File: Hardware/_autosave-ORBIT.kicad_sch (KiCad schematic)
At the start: 52 parts, among them J1 West Connector, J2 East Connector, U1 MCP73031, U10 8MHz, U15 TPS63802DLAR, U16 STM32F030C8Tx, U22 CP2102-GMR

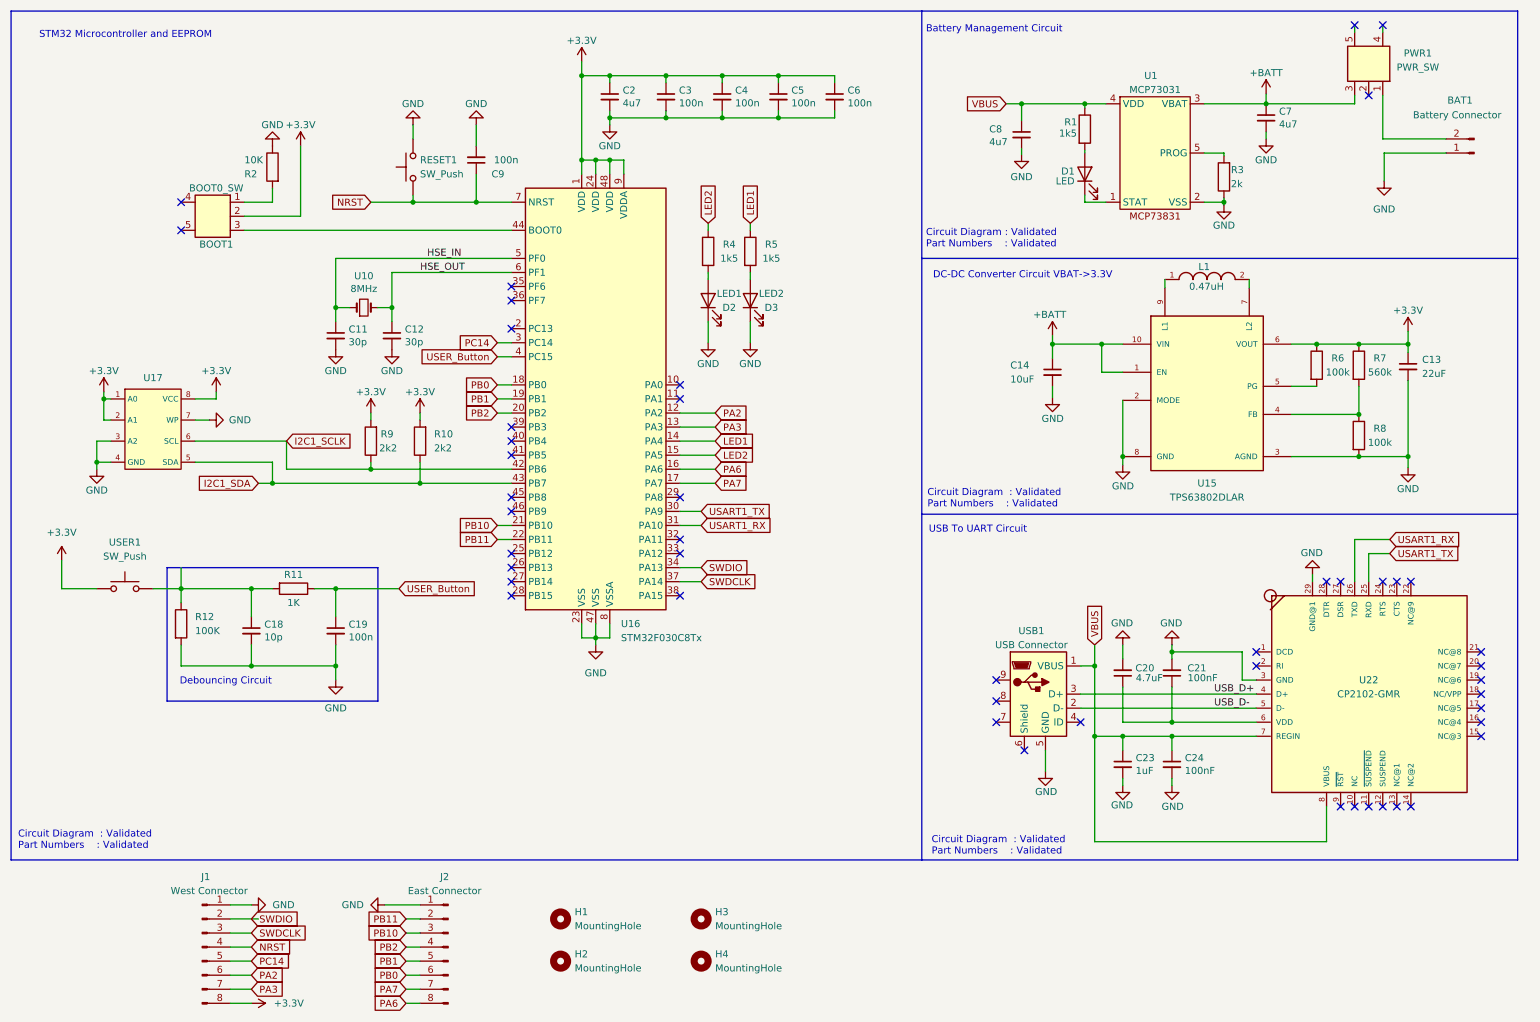
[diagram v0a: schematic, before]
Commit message: all components in the final positioned
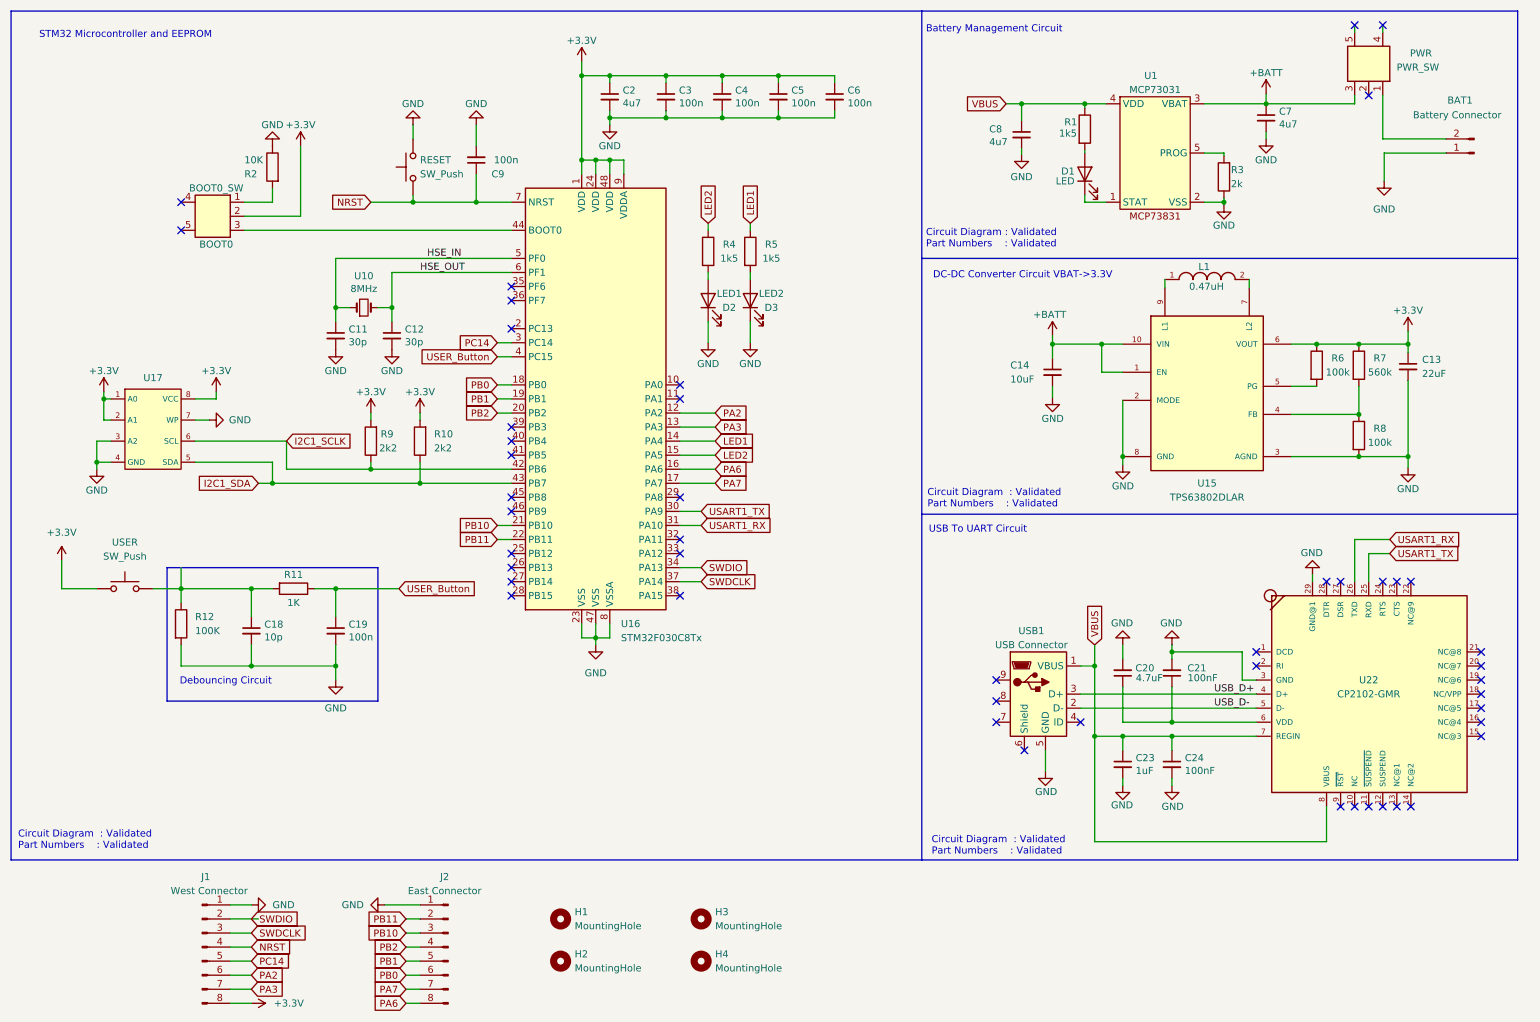
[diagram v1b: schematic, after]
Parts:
- renumbered BOOT1 to BOOT0, PWR1 to PWR, RESET1 to RESET, USER1 to USER
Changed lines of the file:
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@@
   (symbol (lib_id "Korean Hroparts Elec SPDT:K3-1270L-F1") (at 49.53 49.53 0) (mirror y) (unit 1)
     (in_bom yes) (on_board yes) (dnp no)
-    (property "Reference" "BOOT1" (at 49.53 54.61 0)
+    (property "Reference" "BOOT0" (at 49.53 54.61 0)
       (effects (font (size 1.27 1.27)))
     )
@@
       (project "ORBIT"
         (path "/3070b2ed-24f5-4699-8606-a941013223e7"
-          (reference "BOOT1") (unit 1)
+          (reference "BOOT0") (unit 1)
         )
       )
@@
   (symbol (lib_id "Switch:SW_Push") (at 85.09 40.64 90) (unit 1)
     (in_bom yes) (on_board yes) (dnp no) (fields_autoplaced)
-    (property "Reference" "RESET1" (at 86.36 39.37 90)
+    (property "Reference" "RESET" (at 86.36 39.37 90)
       (effects (font (size 1.27 1.27)) (justify right))
     )
@@
       (project "ORBIT"
         (path "/3070b2ed-24f5-4699-8606-a941013223e7"
-          (reference "RESET1") (unit 1)
+          (reference "RESET") (unit 1)
         )
       )
@@
   (symbol (lib_id "Switch:SW_Push") (at 33.02 116.84 0) (unit 1)
     (in_bom yes) (on_board yes) (dnp no) (fields_autoplaced)
-    (property "Reference" "USER1" (at 33.02 108.458 0)
+    (property "Reference" "USER" (at 33.02 108.458 0)
       (effects (font (size 1.27 1.27)))
     )
@@
       (project "ORBIT"
         (path "/3070b2ed-24f5-4699-8606-a941013223e7"
-          (reference "USER1") (unit 1)
+          (reference "USER") (unit 1)
         )
       )
@@
   (symbol (lib_id "Korean Hroparts Elec SPDT:K3-1270L-F1") (at 257.81 22.606 270) (mirror x) (unit 1)
     (in_bom yes) (on_board yes) (dnp no)
-    (property "Reference" "PWR1" (at 269.24 20.066 90)
+    (property "Reference" "PWR" (at 269.24 20.066 90)
       (effects (font (size 1.27 1.27)) (justify right))
     )
@@
       (project "ORBIT"
         (path "/3070b2ed-24f5-4699-8606-a941013223e7"
-          (reference "PWR1") (unit 1)
-        )
-      )
+          (reference "PWR") (unit 1)
+        )
+      )
